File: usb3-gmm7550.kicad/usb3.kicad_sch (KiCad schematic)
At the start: 0 parts

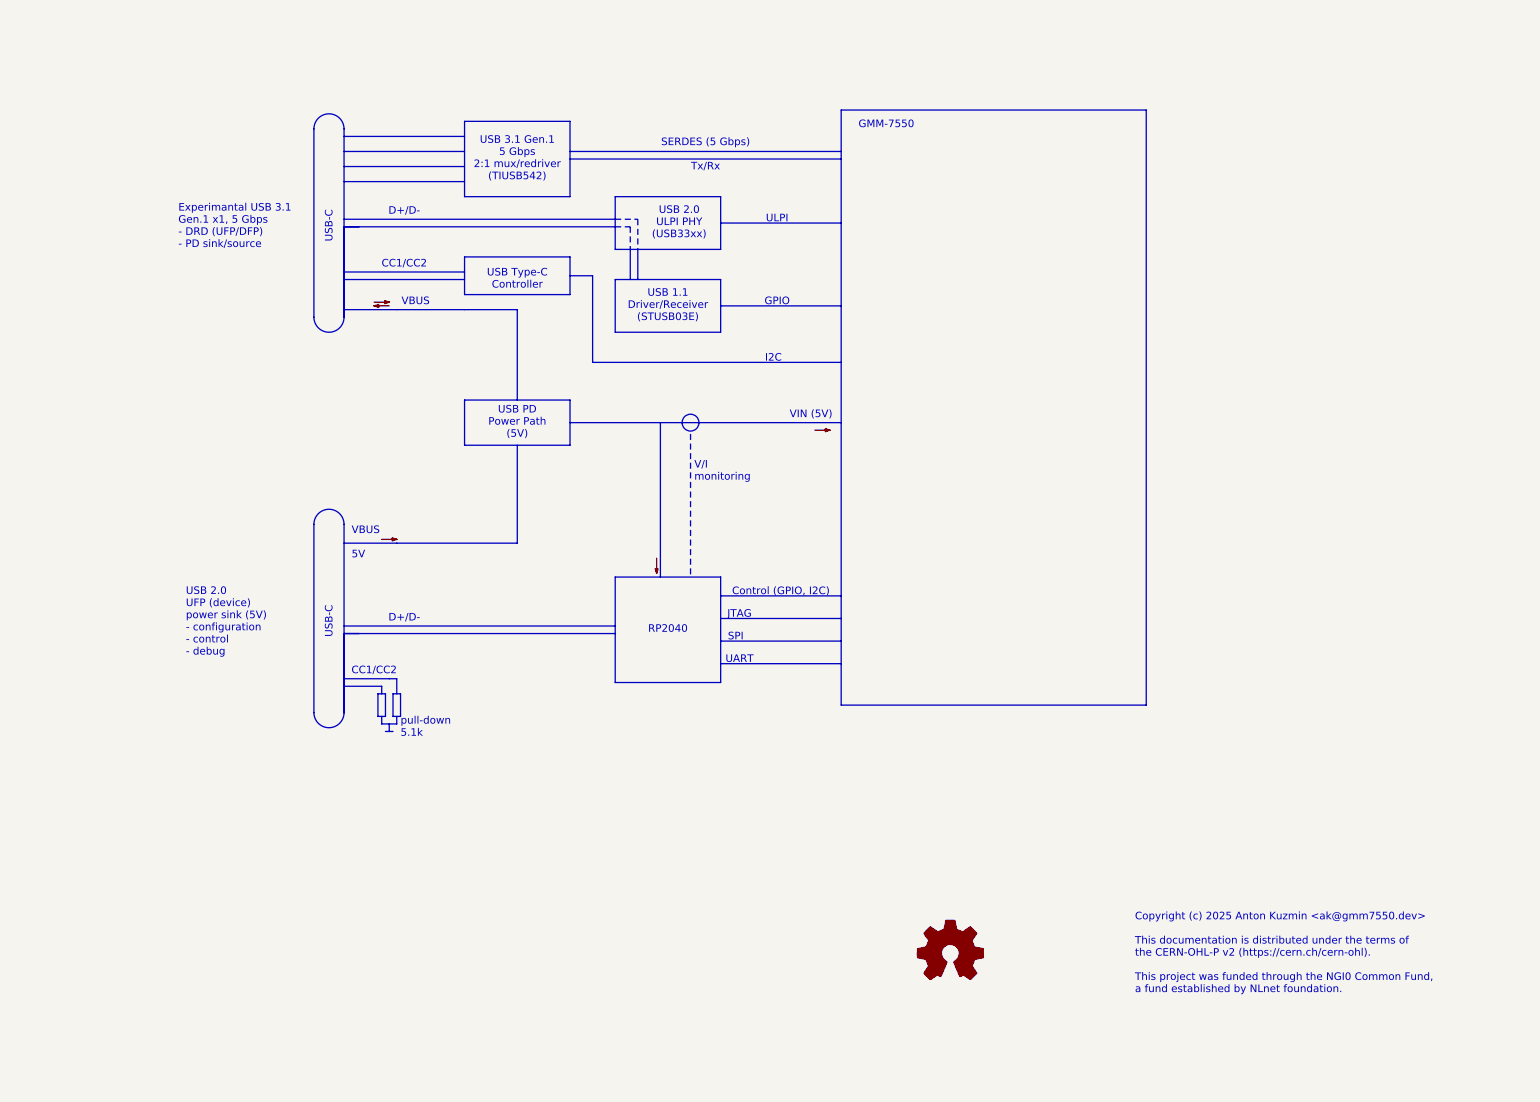
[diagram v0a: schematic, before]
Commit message: Add pages to the USB 3 Adapter schematic and new project symbols
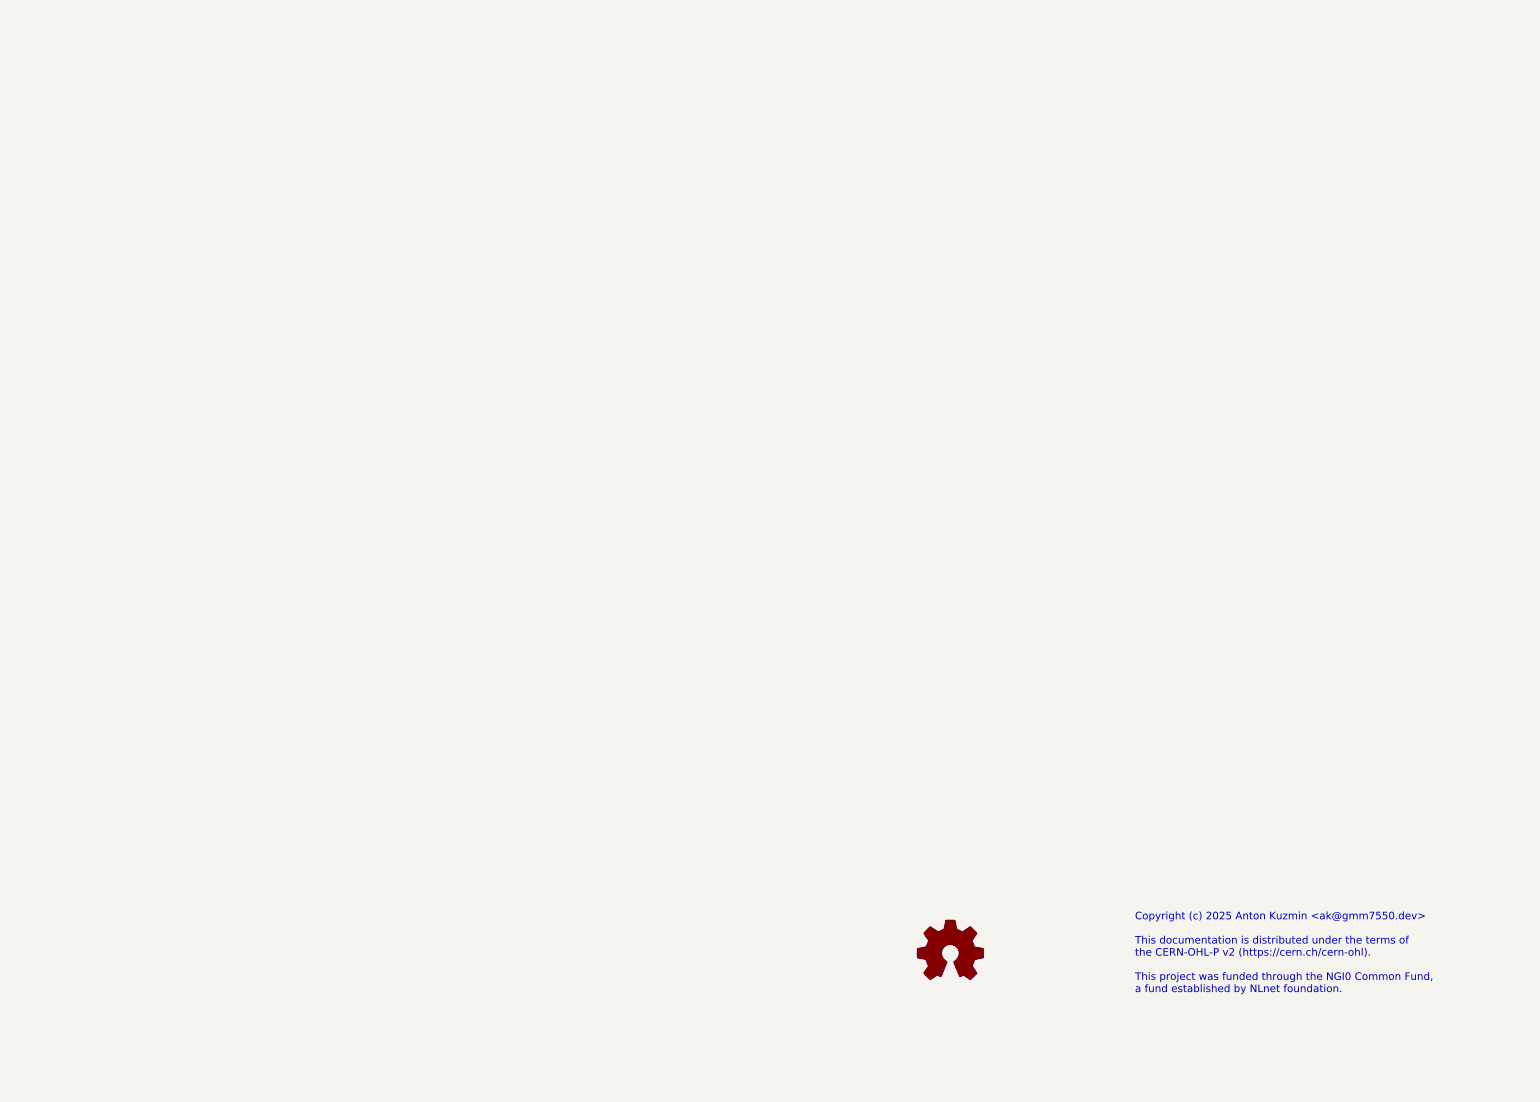
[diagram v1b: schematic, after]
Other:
- note removed: "CC1/CC2"
- note removed: "Control (GPIO, I2C)"
- note removed: "D+/D-"
- note removed: "Experimantal USB 3.1 Gen.1 x1, 5 Gbps - DRD (UFP/DFP) - PD sink/source"
- note removed: "GMM-7550"
- note removed: "GPIO"
- note removed: "I2C"
- note removed: "JTAG"
- note removed: "RP2040"
- note removed: "SERDES (5 Gbps) Tx/Rx"
- note removed: "SPI"
- note removed: "UART"
- note removed: "ULPI"
- note removed: "USB 1.1 Driver/Receiver (STUSB03E)"
- note removed: "USB 2.0 UFP (device) power sink (5V) - configuration - control - debug"
- note removed: "USB 2.0 ULPI PHY (USB33xx)"
- note removed: "USB 3.1 Gen.1 5 Gbps 2:1 mux/redriver (TIUSB542)"
- note removed: "USB PD Power Path (5V)"
- note removed: "USB Type-C Controller"
- note removed: "USB-C"
- note removed: "V/I monitoring"
- note removed: "VBUS"
- note removed: "VBUS 5V"
- note removed: "VIN (5V)"
- note removed: "pull-down 5.1k"

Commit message: USB 3 adapter schematic -- WIP
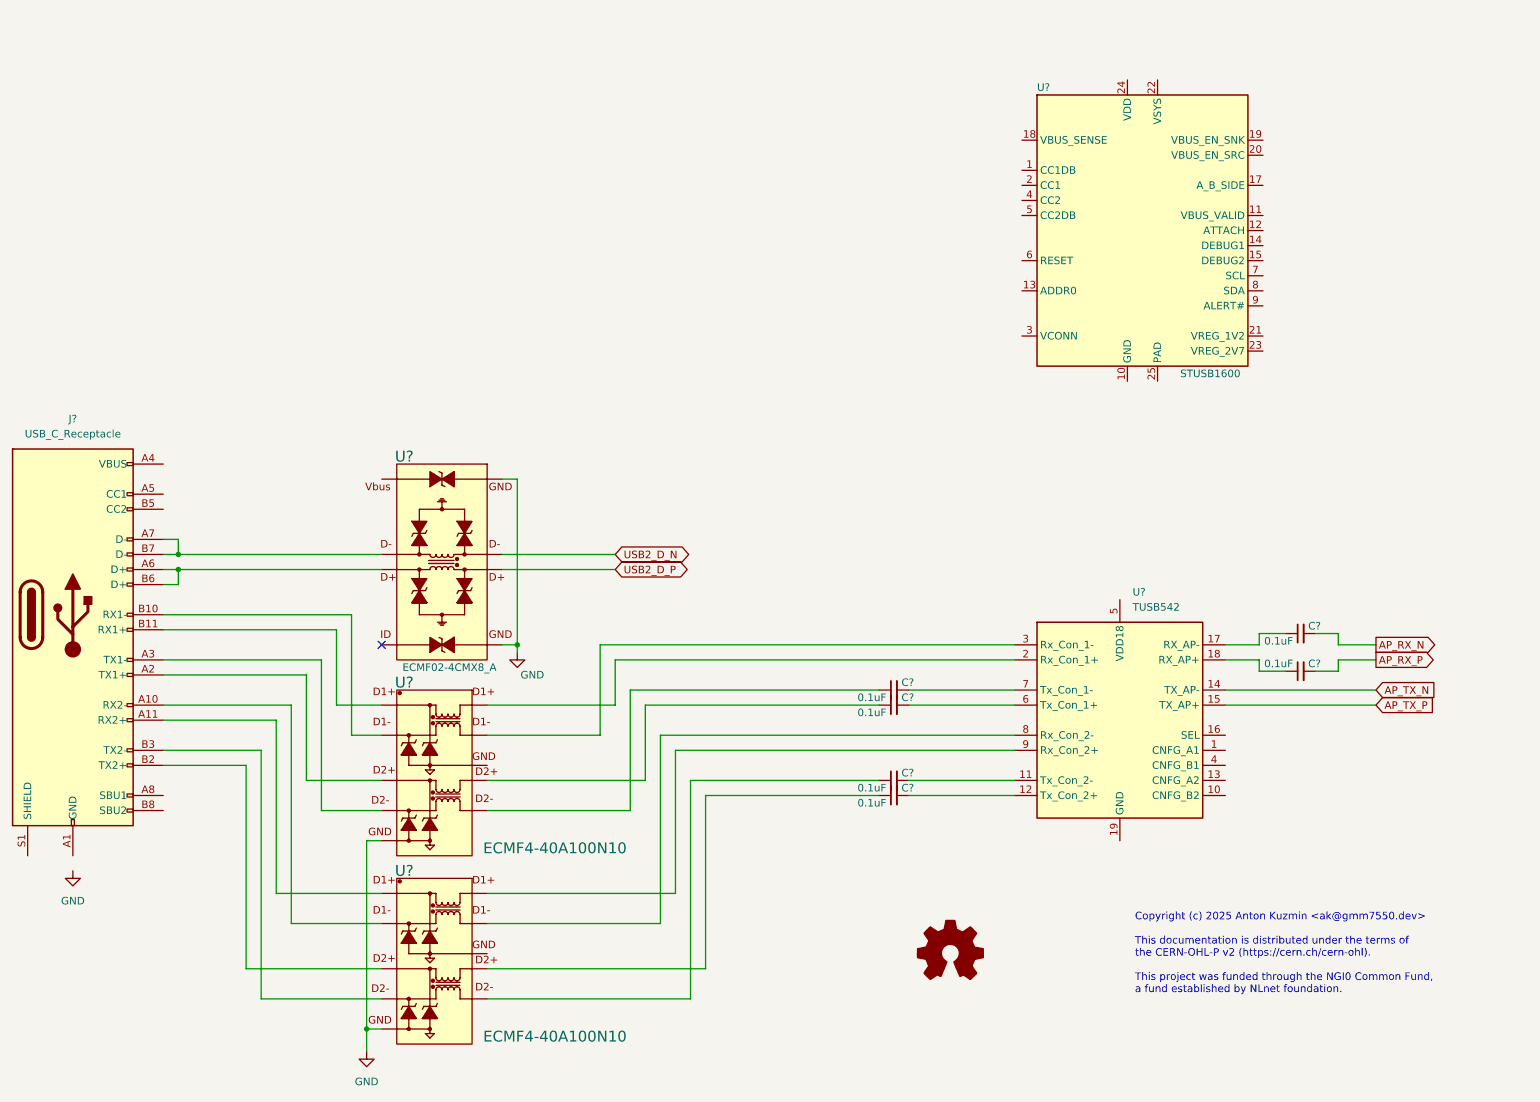
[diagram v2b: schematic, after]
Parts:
- added C? (x6): 0.1uF, Capacitor_SMD:C_0402_1005Metric, symbol Device:C_Small
- added J?: USB_C_Receptacle, symbol Connector:USB_C_Receptacle
- added U?: STUSB1600, Package_DFN_QFN:QFN-24-1EP_4x4mm_P0.5mm_EP2.7x2.7mm_ThermalVias, symbol usb3-gmm7550:STUSB1600
- added U? (x2): ECMF4-40A100N10, ST_QFN40P220X135X50-10L, symbol usb3-gmm7550:ECMF4-40A100N10
- added U?: TUSB542, usb3-gmm7550:Texas_X2QFN-18-1EP_2x2.4mm_P0.4mm_EP1x1.4mm_ThermalVias, symbol usb3-gmm7550:TUSB542
- added U?: ECMF02-4CMX8_A, ST_QFN50P255X125X55-8L, symbol usb3-gmm7550:ECMF02-4CMX8
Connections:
- new net: C?.1, U?.17 (RX_AP-)
- new net: C?.1, U?.6 (D2-1) (x2)
- new net: C?.2, U?.7 (Tx_Con_1-)
- new net: J?.B11 (RX1+), U?.1 (D1+)
- new net: U?.10 (D1+1), U?.2 (Rx_Con_1+)
- new net: J?.B10 (RX1-), U?.2 (D1-)
- new net: J?.A2 (TX1+), U?.4 (D2+)
- new net: J?.A3 (TX1-), U?.5 (D2-)
- new net: C?.1, U?.7 (D2+1) (x2)
- new net: U?.3 (Rx_Con_1-), U?.9 (D1-1)
- new net: J?.A11 (RX2+), U?.1 (D1+)
- new net: U?.10 (D1+1), U?.9 (Rx_Con_2+)
- new net: J?.A10 (RX2-), U?.2 (D1-)
- new net: J?.B2 (TX2+), U?.4 (D2+)
- new net: J?.B3 (TX2-), U?.5 (D2-)
- new net: U?.8 (Rx_Con_2-), U?.9 (D1-1)
- new net: C?.2, U?.11 (Tx_Con_2-)
- new net: C?.2, U?.12 (Tx_Con_2+)
- new net: C?.1, U?.18 (RX_AP+)
- new net: C?.2, U?.6 (Tx_Con_1+)
- new net: J?.A7 (D-), J?.B7 (D-), U?.2 (D-)
- new net: J?.A6 (D+), J?.B6 (D+), U?.3 (D+)
- new net: J?.A1 (GND), J?.A12 (GND), J?.B1 (GND), J?.B12 (GND)
- new net: J?.A4 (VBUS), J?.A9 (VBUS), J?.B4 (VBUS), J?.B9 (VBUS)
- new net AP_RX_N: C?.2
- new net AP_RX_P: C?.2
- new net AP_TX_N: U?.14 (TX_AP-)
- new net AP_TX_P: U?.15 (TX_AP+)
- new net GND: U?.3 (GND), U?.3 (GND), U?.5 (GND), U?.8 (GND1)
- new net USB2_D_N: U?.7 (D-1)
- new net USB2_D_P: U?.6 (D+1)
- no-connect marks 0 -> 1

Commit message: USB 3 adapter schematic -- WIP: new components and footprints
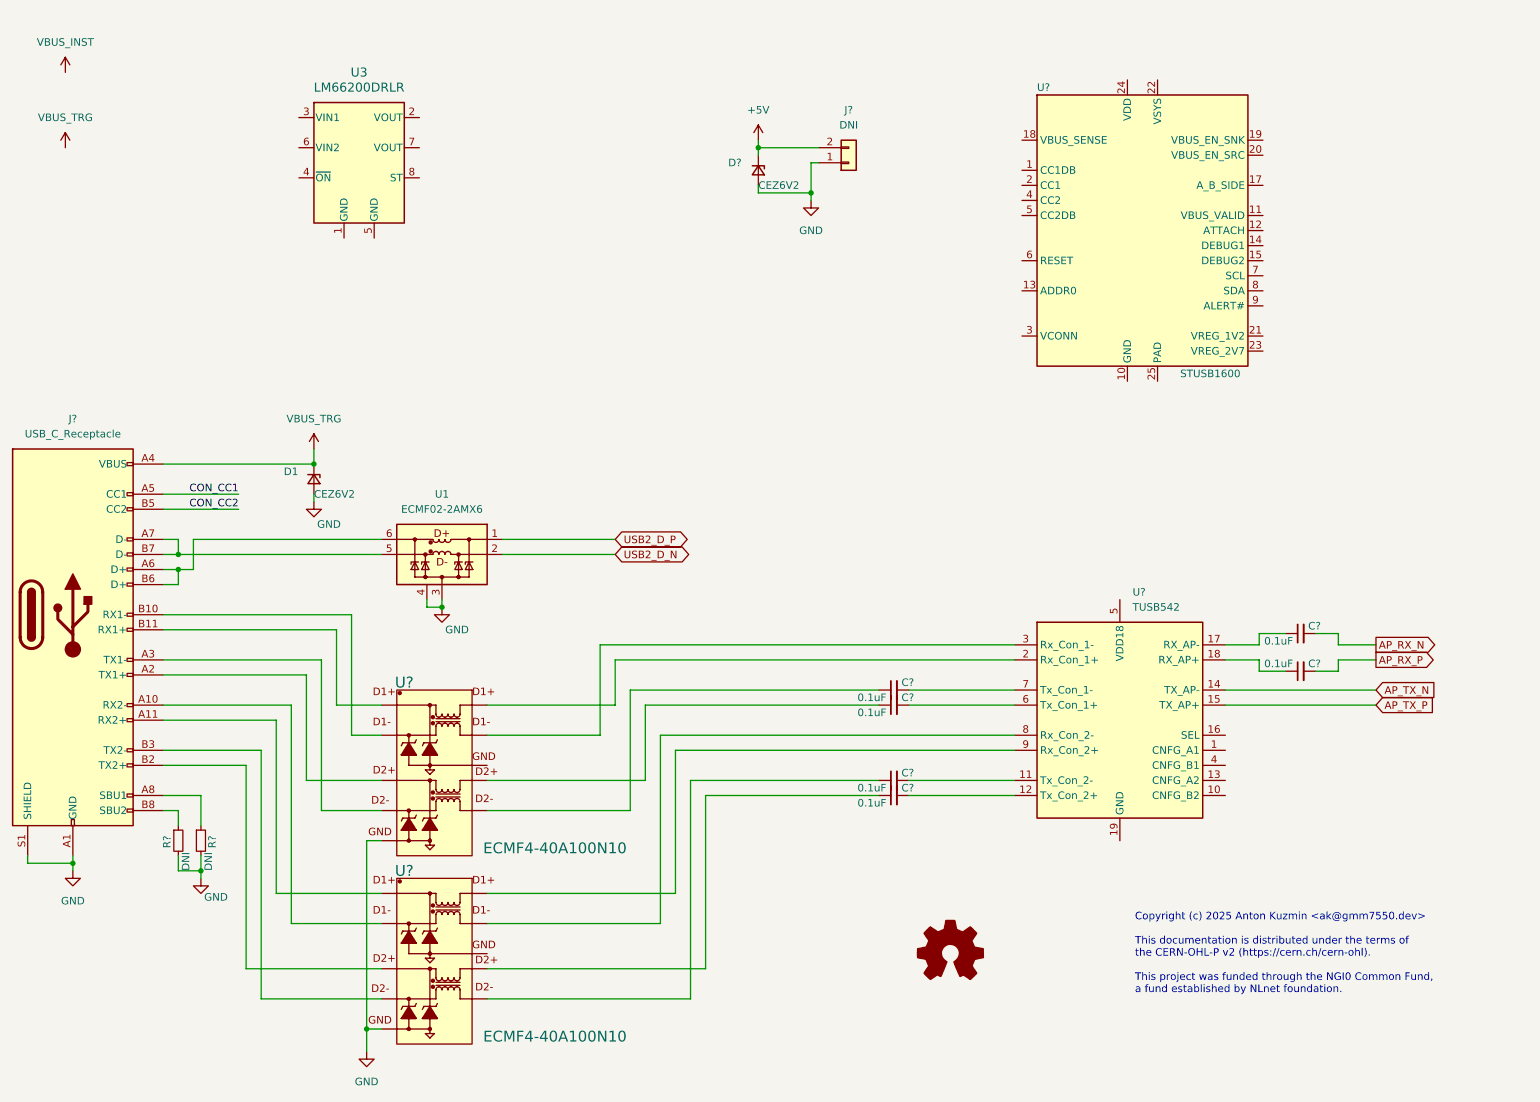
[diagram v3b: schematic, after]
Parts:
- removed U?: ECMF02-4CMX8_A, ST_QFN50P255X125X55-8L, symbol usb3-gmm7550:ECMF02-4CMX8
- added D1, D?: CEZ6V2, Diode_SMD:D_SOD-523, symbol Device:D_Zener_Small
- added J?: DNI, Connector_Molex:Molex_Micro-Fit_3.0_43045-0200_2x01_P3.00mm_Horizontal, symbol Connector_Generic:Conn_01x02
- added R? (x2): DNI, Resistor_SMD:R_0402_1005Metric, symbol Device:R_Small
- added U1: ECMF02-2AMX6, Package_DFN_QFN:ST_UQFN-6L_1.5x1.7mm_P0.5mm, symbol Power_Protection:ECMF02-2AMX6
- added U3: LM66200DRLR, SOT-5X3_DRL_TEX, symbol usb3-gmm7550:LM66200DRLR
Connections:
- net GND: now also J?.A1 (GND), J?.A12 (GND), J?.B1 (GND), J?.B12 (GND), J?.S1 (SHIELD), D1.2 (A), D?.2 (A), J?.1 (Pin_1), R?.2, R?.2, U1.3 (GND), U1.4 (NC)
- net USB2_D_N: now also U1.2 (D-_in)
- net USB2_D_P: now also U1.1 (D+_in)
- net at J?.A7 (D-), J?.B7 (D-): now also U1.5 (D-_out)
- net at J?.A6 (D+), J?.B6 (D+): now also U1.6 (D+_out)
- net VBUS_TRG: now reaches J?.A4 (VBUS), J?.A9 (VBUS), J?.B4 (VBUS), J?.B9 (VBUS)
- net VBUS_TRG: now also D1.1 (K)
- net CON_CC1: now reaches J?.A5 (CC1)
- net at J?.A8 (SBU1): now also R?.1
- net CON_CC2: now reaches J?.B5 (CC2)
- net at J?.B8 (SBU2): now also R?.1
- new net +5V: D?.1 (K), J?.2 (Pin_2)
- no-connect marks 1 -> 0
